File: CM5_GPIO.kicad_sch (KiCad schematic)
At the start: 17 parts, among them J1 USB3_A, J14 JST_SHBM04B-SRSS-TB, J2 Conn_02x07_Odd_Even, J3 Conn_01x03, J8 THD-20-R, SW1 Right angle Tact button, U5 74LVC1G07SE-7

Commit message: Board development
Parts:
- removed J1: USB3_A, CM5IO:MTCONN_UBAF30-D2011, symbol CM5IO:USB3_A

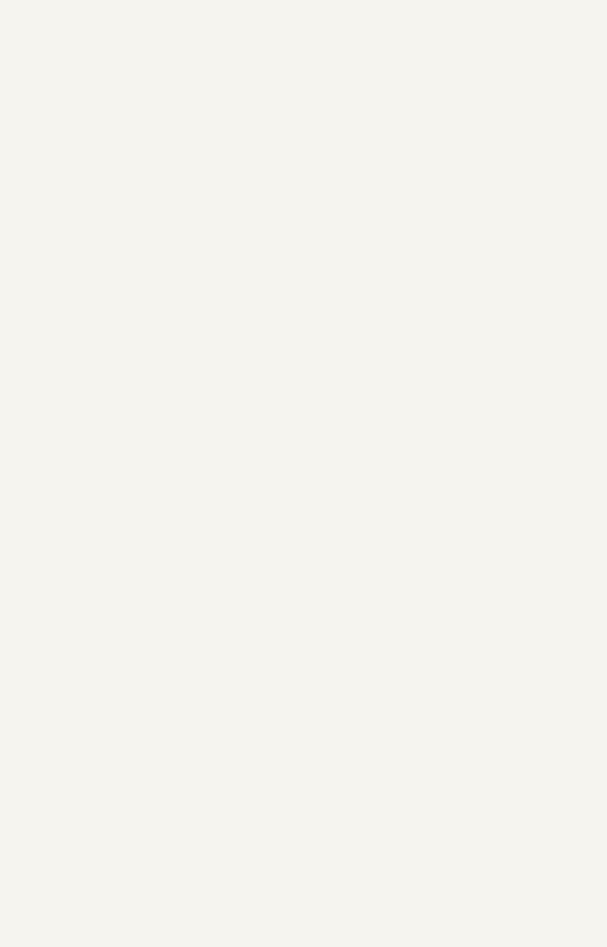
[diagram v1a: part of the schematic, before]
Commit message: Added USB SS type A, thinking of replacing it in the future with USB type-c
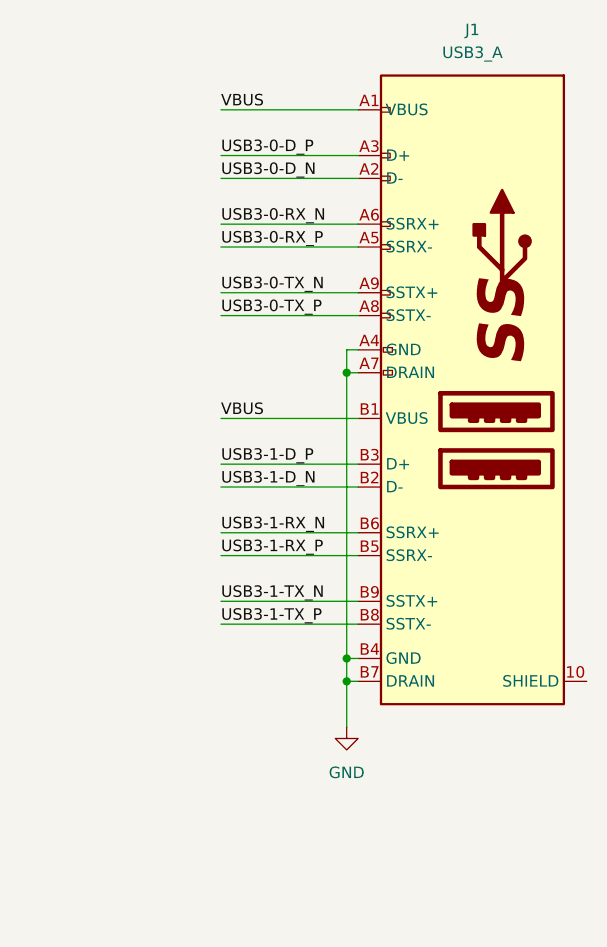
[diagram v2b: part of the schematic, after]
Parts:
- added J1: USB3_A, CM5IO:MTCONN_UBAF30-D2011, symbol CM5IO:USB3_A
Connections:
- net GND: now also J1.A4 (GND), J1.A7 (DRAIN), J1.B4 (GND), J1.B7 (DRAIN)
- new net USB3-0-D_N: J1.A2 (D-)
- new net USB3-0-D_P: J1.A3 (D+)
- new net USB3-0-RX_N: J1.A6 (SSRX+)
- new net USB3-0-RX_P: J1.A5 (SSRX-)
- new net USB3-0-TX_N: J1.A9 (SSTX+)
- new net USB3-0-TX_P: J1.A8 (SSTX-)
- new net USB3-1-D_N: J1.B2 (D-)
- new net USB3-1-D_P: J1.B3 (D+)
- new net USB3-1-RX_N: J1.B6 (SSRX+)
- new net USB3-1-RX_P: J1.B5 (SSRX-)
- new net USB3-1-TX_N: J1.B9 (SSTX+)
- new net USB3-1-TX_P: J1.B8 (SSTX-)
- new net VBUS: J1.A1 (VBUS), J1.B1 (VBUS)
